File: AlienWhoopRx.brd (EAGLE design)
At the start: 12 x 16 mm, 16 parts, among them U1 XN297L, Y1 16MHZ

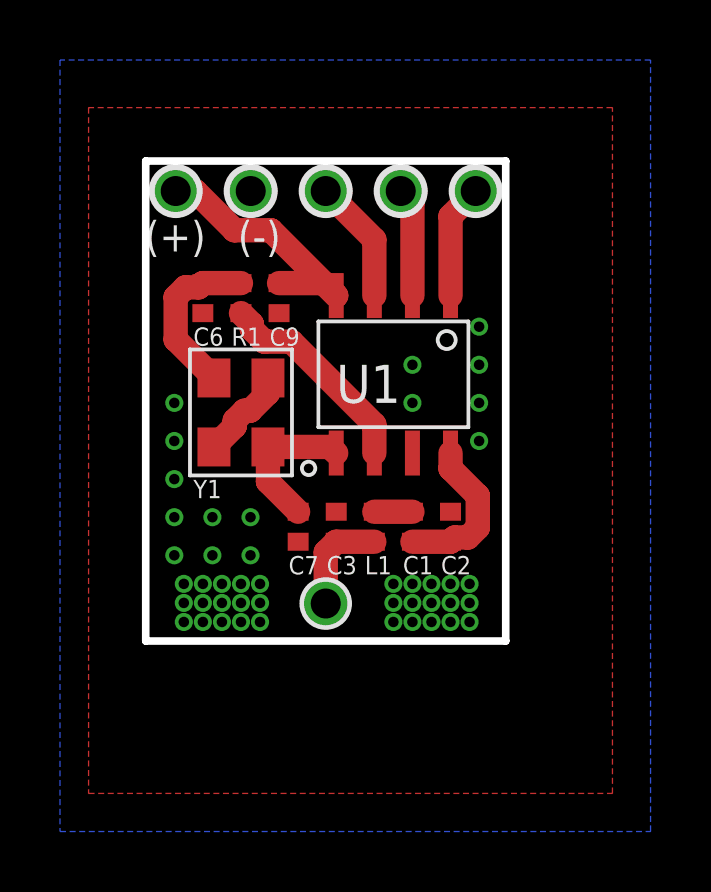
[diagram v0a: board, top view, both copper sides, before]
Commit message: Shrunk overall dimensions. Second draft as ordered from OSH Park on 2018-09-06
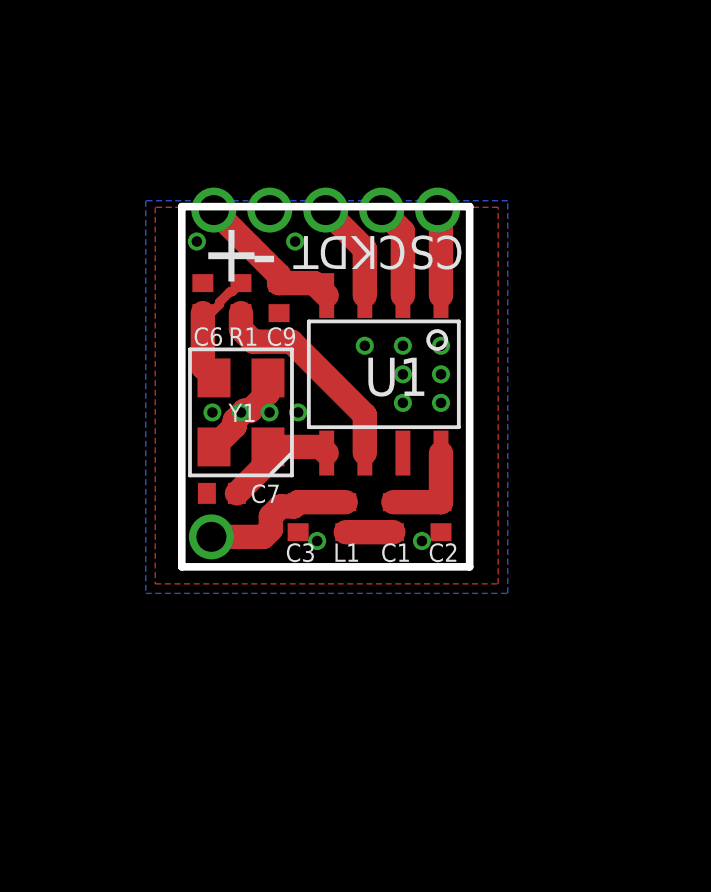
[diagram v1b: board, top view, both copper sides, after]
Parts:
- moved U$6 4.41 mm to (2.19, 3.47)
- moved C7 2.77 mm to (2.54, 4.92), turned to 180 degrees
- moved 3.3V2 1.42 mm to (2.27, 14.4)
- moved SPI_CS 1.42 mm to (9.73, 14.4)
- moved C3 1.31 mm to (5.08, 4.13), turned to 270 degrees
- moved L1 1.00 mm to (6.67, 4.13), turned to 90 degrees
- moved GND23 0.90 mm to (4.13, 14.4)
- moved U$13 0.90 mm to (7.87, 14.4)
- moved C1 0.71 mm to (8.26, 4.13), turned to 270 degrees
- moved U$14 0.63 mm to (6.00, 14.4)
- moved C2 0.45 mm to (9.84, 4.13), turned to 270 degrees
- moved U1 0.32 mm to (7.94, 8.89)
- turned C6 to 90 degrees
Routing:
- net 3.3V: track 8.87 -> 5.10 mm
- net XC1: track 6.40 -> 4.02 mm
- net ANT_OUT: track 5.24 -> 3.22 mm
- net ANT: track 3.47 -> 5.21 mm
- net XC2R: track 5.59 -> 4.04 mm
- net CSN: track 3.83 -> 2.90 mm
- net DAT: track 4.16 -> 3.39 mm
- net SCK: track 3.65 -> 3.14 mm
- net GND: track 3.66 -> 3.16 mm, vias 46 -> 16
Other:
- board size 12 x 16 mm -> 9.6 x 12 mm
- board text added: "+"
- board text added: "-"
- board text added: "CK"
- board text added: "CS"
- board text added: "DT"
- board text removed: "(+)"
- board text removed: "(-)"
